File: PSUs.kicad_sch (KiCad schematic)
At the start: 33 parts, among them J12 Barrel_Jack, J13 Conn_01x02_Female, Q3 DMP3013SFV-7, U8 AP64501SP-13

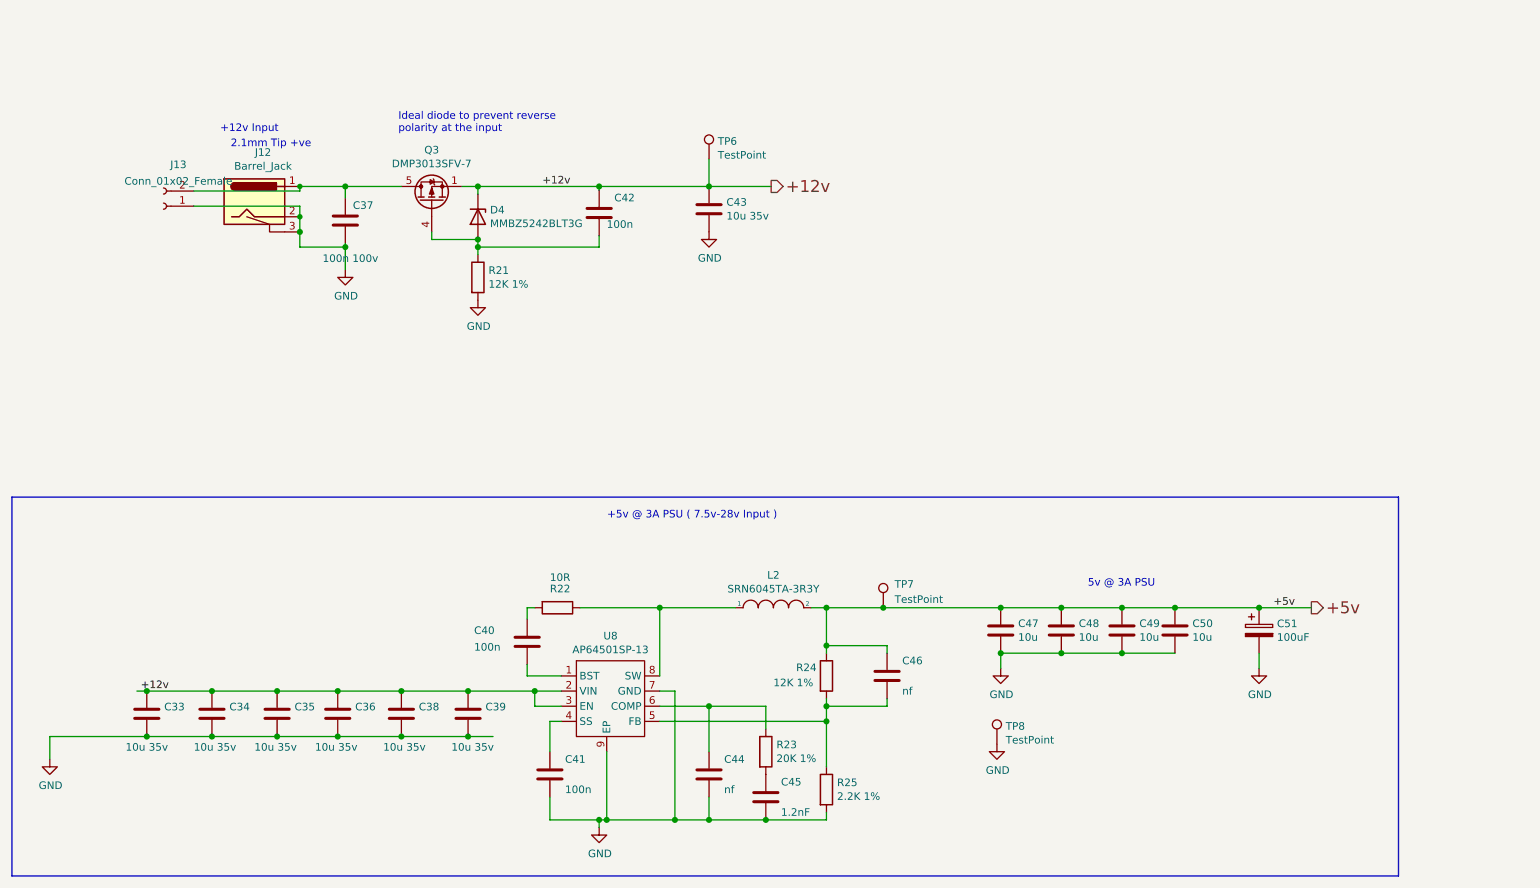
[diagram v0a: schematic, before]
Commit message: Initial layout and all parts added. Some pins still not connected to power
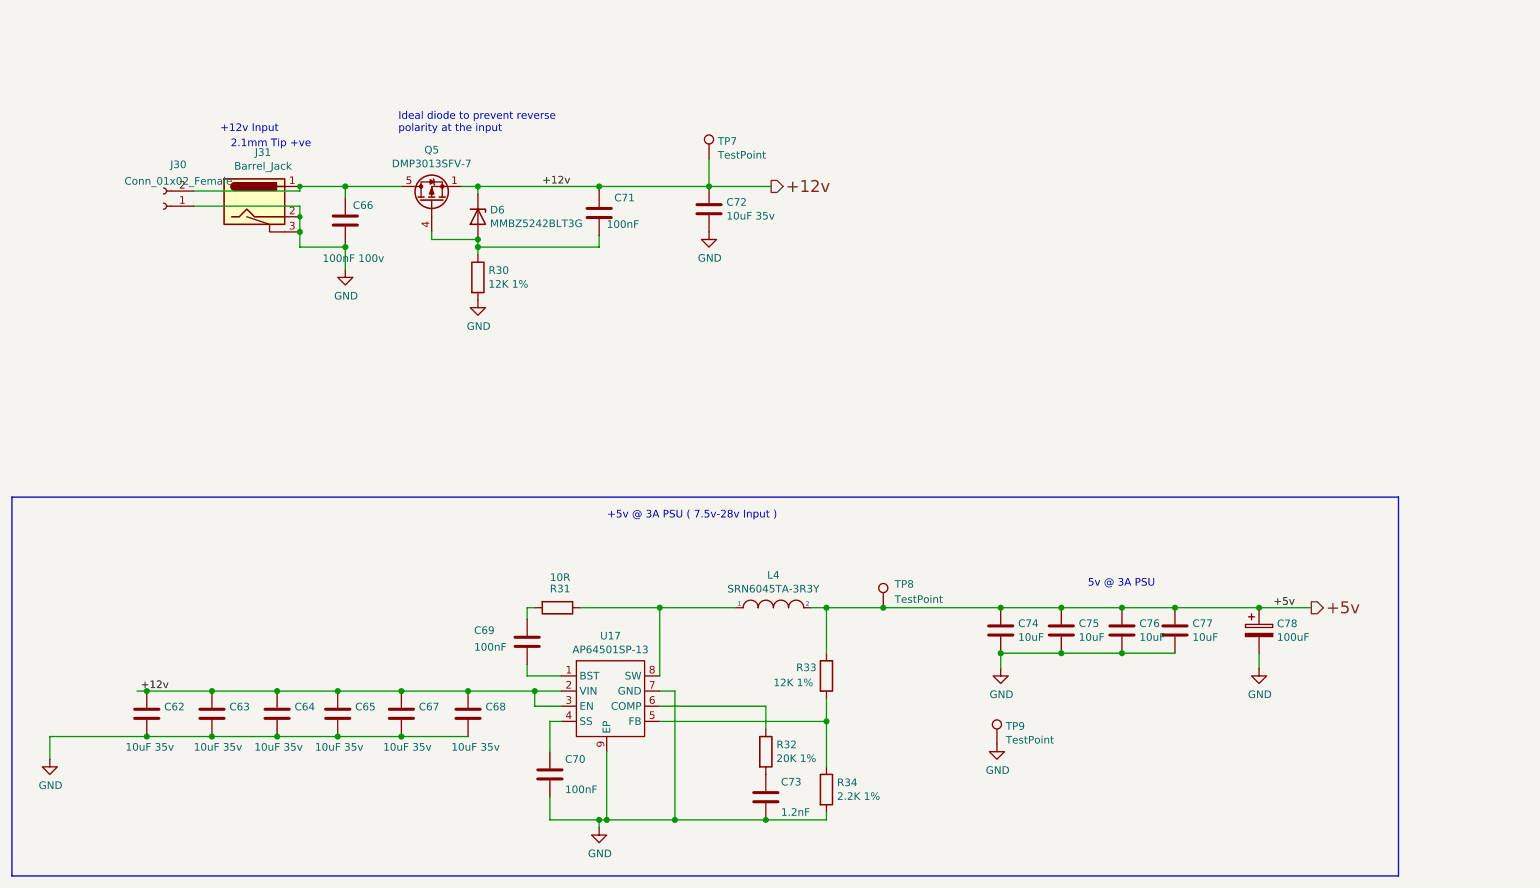
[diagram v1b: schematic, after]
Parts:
- removed C44, C46: nf, Capacitor_SMD:C_0402_1005Metric, symbol Device:C
- C62: renamed from C33; value 10u 35v -> 10uF 35v
- C63: renamed from C34; value 10u 35v -> 10uF 35v
- C64: renamed from C35; value 10u 35v -> 10uF 35v
- C65: renamed from C36; value 10u 35v -> 10uF 35v
- C66: renamed from C37; value 100n 100v -> 100nF 100v
- C67: renamed from C38; value 10u 35v -> 10uF 35v
- C68: renamed from C39; value 10u 35v -> 10uF 35v
- C69: renamed from C40; value 100n -> 100nF
- C70: renamed from C41; value 100n -> 100nF
- C71: renamed from C42; value 100n -> 100nF
- C72: renamed from C43; value 10u 35v -> 10uF 35v
- C74: renamed from C47; value 10u -> 10uF
- C75: renamed from C48; value 10u -> 10uF
- C76: renamed from C49; value 10u -> 10uF
- C77: renamed from C50; value 10u -> 10uF
- renumbered C45 to C73, C51 to C78, D4 to D6, J13 to J30, J12 to J31, L2 to L4, Q3 to Q5, R21 to R30, R22 to R31, R23 to R32, R24 to R33, R25 to R34, TP6 to TP7, TP7 to TP8, TP8 to TP9, U8 to U17

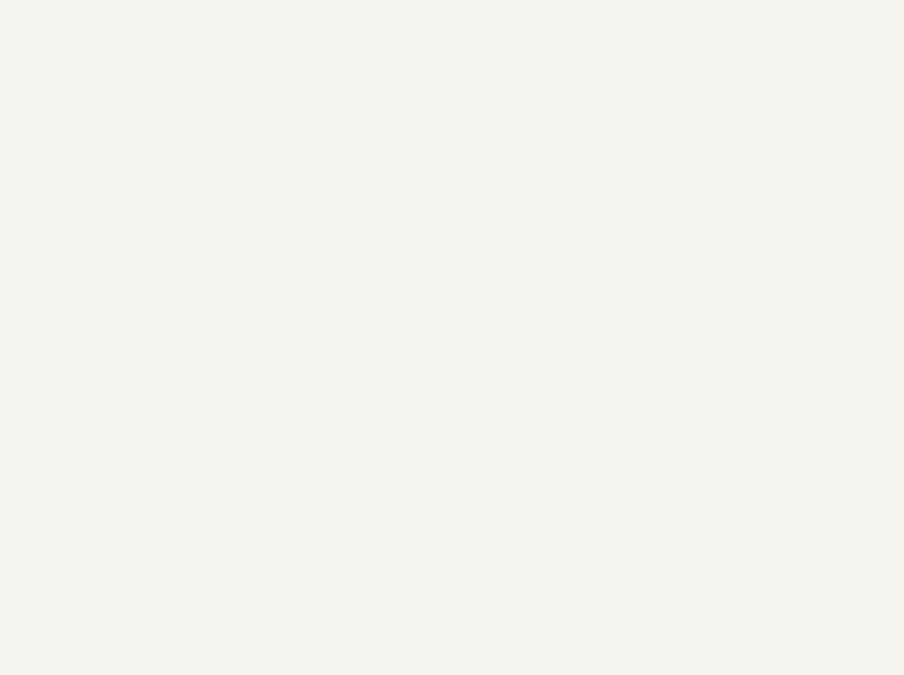
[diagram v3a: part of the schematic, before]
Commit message: Added usb to ethernet and changed mcu to stm32g4
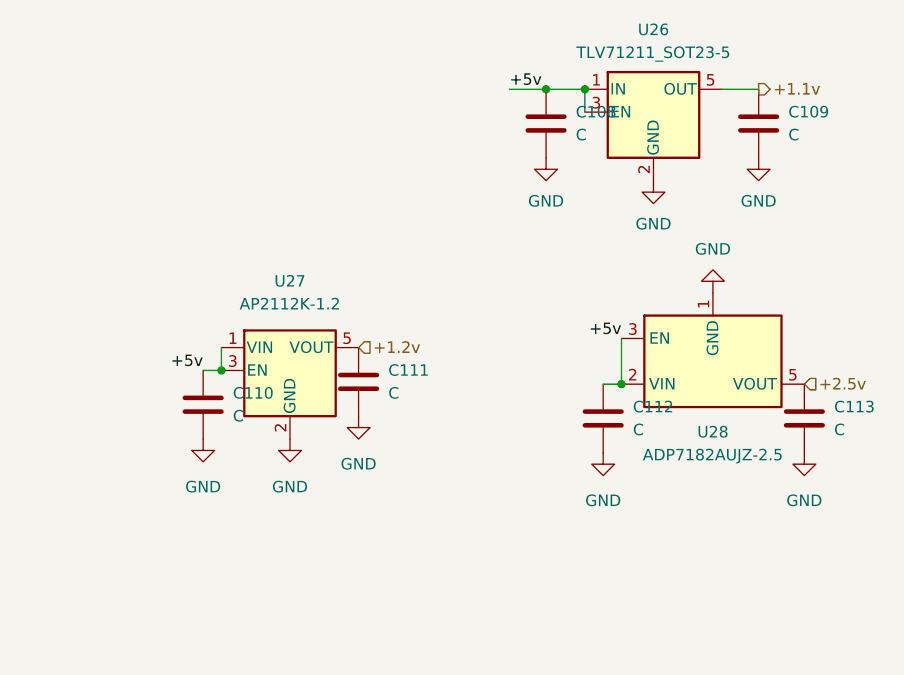
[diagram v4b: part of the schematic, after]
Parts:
- added C108, C109, C110, C111, C112, C113: C, Capacitor_SMD:C_0402_1005Metric, symbol Device:C
- added U26: TLV71211_SOT23-5, Package_TO_SOT_SMD:SOT-23-5, symbol Regulator_Linear:TLV71211_SOT23-5
- added U27: AP2112K-1.2, Package_TO_SOT_SMD:SOT-23-5, symbol Regulator_Linear:AP2112K-1.2
- added U28: ADP7182AUJZ-2.5, Package_TO_SOT_SMD:TSOT-23-5, symbol Regulator_Linear:ADP7182AUJZ-2.5
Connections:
- net +5v: now also C108.1, C110.1, C112.1, U26.1 (IN), U26.3 (EN), U27.1 (VIN), U27.3 (EN), U28.2 (VIN), U28.3 (EN)
- net GND: now also C108.2, C109.2, C110.2, C111.2, C112.2, C113.2, U26.2 (GND), U27.2 (GND), U28.1 (GND)
- new net +1.1v: C109.1, U26.5 (OUT)
- new net +1.2v: C111.1, U27.5 (VOUT)
- new net +2.5v: C113.1, U28.5 (VOUT)
